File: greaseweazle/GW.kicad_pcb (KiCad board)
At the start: 2 copper layers, 61 x 22.9 mm, 8 parts, among them P5 POWER

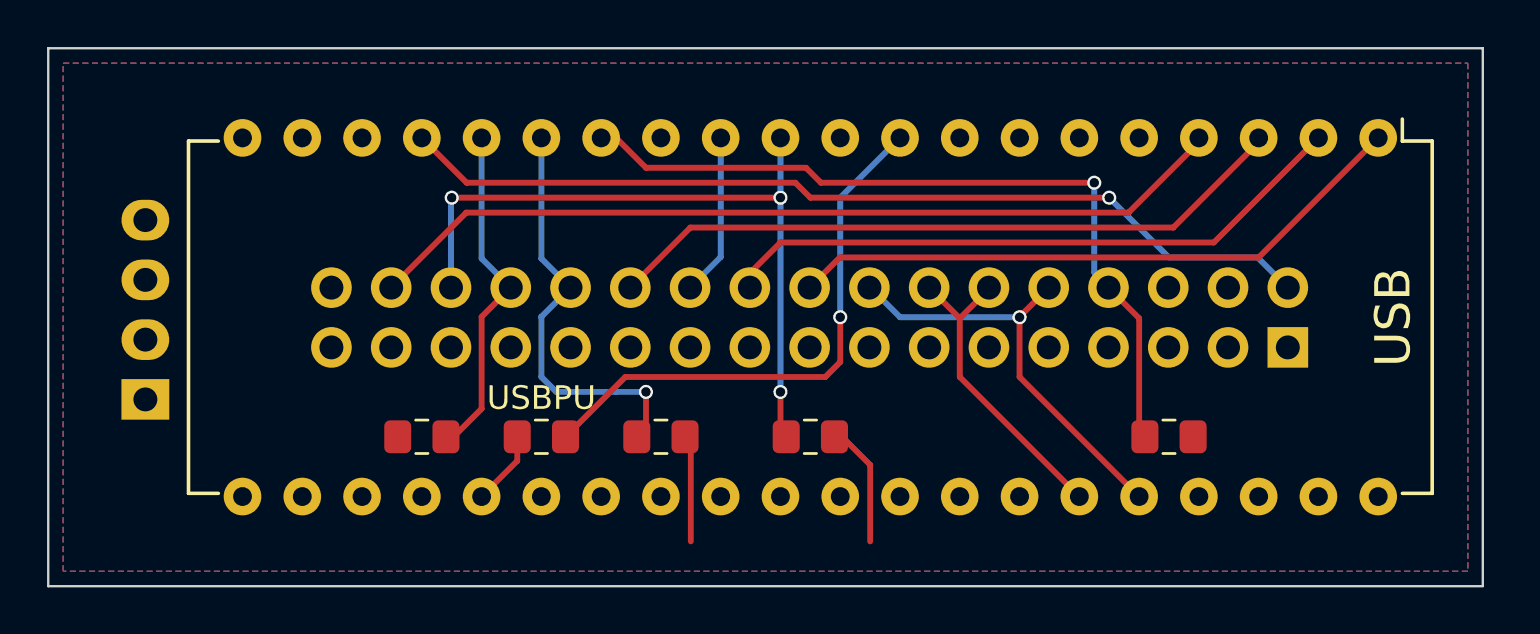
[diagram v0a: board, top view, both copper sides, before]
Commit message: Update to KiCAD 6; added 3D model of the BluePill
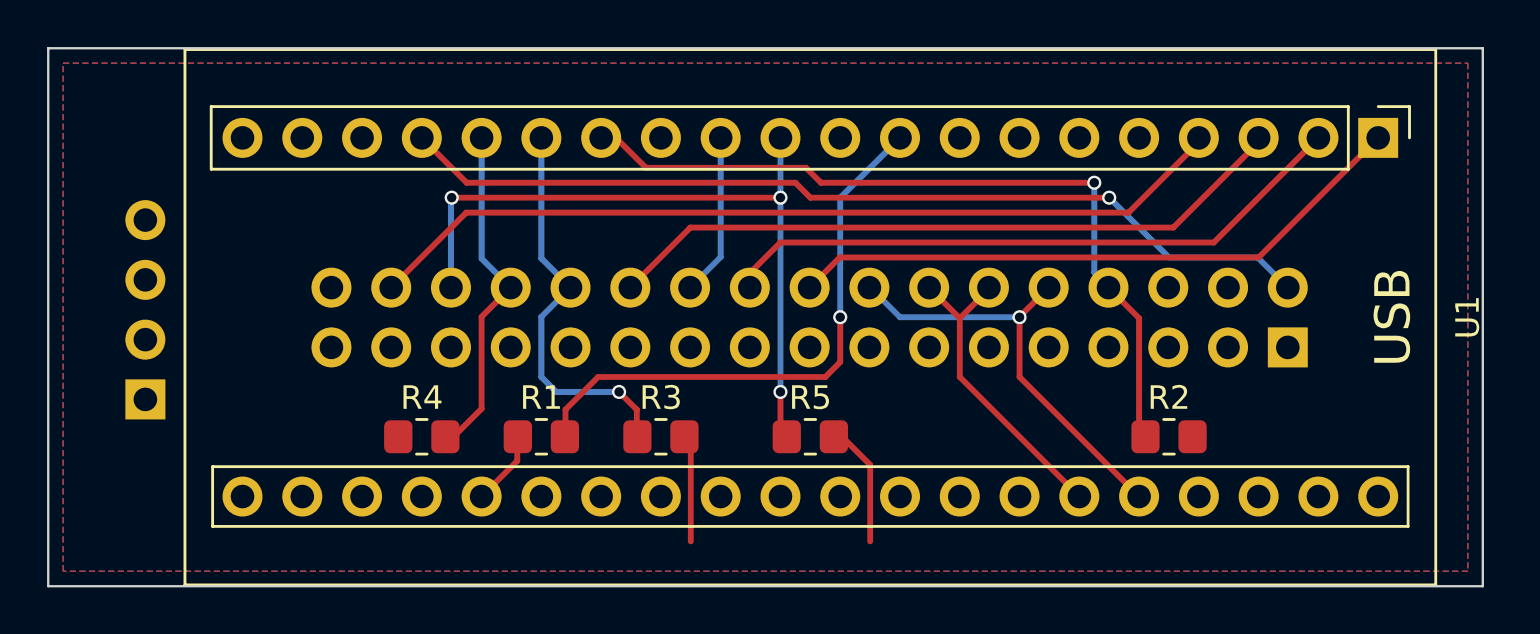
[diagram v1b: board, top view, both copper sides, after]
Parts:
- removed ?: , Housings_DIP:DIP-40_W15.24mm
- added U1: YAAJ_BluePill_Part_Like, Footprints:YAAJ_BluePill_2, F.Cu at (173.4, 97.8)
- P5: footprint Pin_Headers:Pin_Header_Straight_1x04 -> Connector_PinHeader_2.54mm:PinHeader_1x04_P2.54mm_Vertical
- P7: renamed from ?; value (none) -> FLOPPY; footprint Pin_Headers:Pin_Header_Straight_2x17 -> Connector_PinHeader_2.54mm:PinHeader_2x17_P2.54mm_Vertical
- R1: renamed from USBPU; footprint Resistor_SMD:R_0805_2012Metric_Pad1.15x1.40mm_HandSolder -> Resistor_SMD:R_0805_2012Metric_Pad1.20x1.40mm_HandSolder
- R2, R3, R4, R5: renamed from ?; footprint Resistor_SMD:R_0805_2012Metric_Pad1.15x1.40mm_HandSolder -> Resistor_SMD:R_0805_2012Metric_Pad1.20x1.40mm_HandSolder
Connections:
- P5 pad 1: (no net) -> unconnected-(P5-Pad1)
- P7 pad 34: (no net) -> unconnected-(P7-Pad34)
- P7 pad 4: (no net) -> unconnected-(P7-Pad4)
- P7 pad 6: (no net) -> unconnected-(P7-Pad6)
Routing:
- net /_TRK0: track 18.0 -> 17.0 mm
- net /USB_DP: track 23.6 -> 24.2 mm
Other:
- net class Default removed
- net class PowIn removed
- net class Power removed
